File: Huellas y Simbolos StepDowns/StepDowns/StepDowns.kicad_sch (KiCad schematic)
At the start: 4 parts

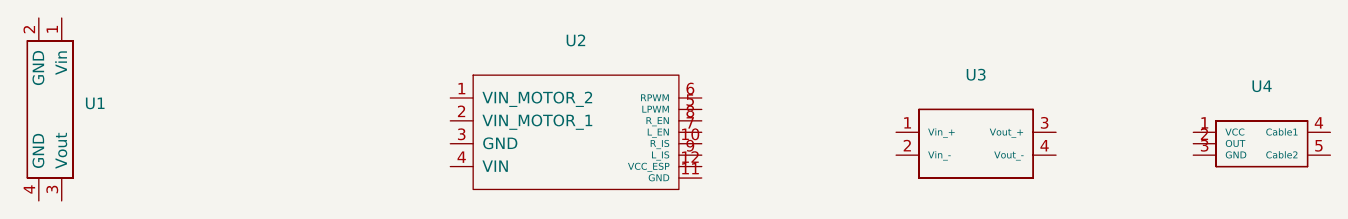
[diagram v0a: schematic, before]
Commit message: Se comenzó con la PCB para SALUS III
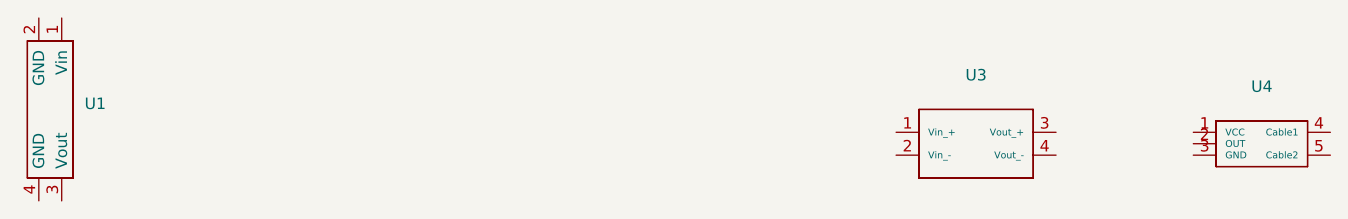
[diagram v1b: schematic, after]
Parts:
- removed U2: ~, Driver_Del_Motor:Driver_Motor, symbol Driver_Del_Motor:Driver_Motor
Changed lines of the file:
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@@
 	(paper "A4")
-	(symbol
-		(lib_id "Driver_Del_Motor:Driver_Motor")
-		(at 167.64 96.52 0)
-		(unit 1)
-		(exclude_from_sim no)
-		(in_bom yes)
-		(on_board yes)
-		(dnp no)
-		(fields_autoplaced yes)
-		(property "Reference" "U2"
-			(at 167.64 85.09 0)
-			(effects
-				(font
-					(size 1.27 1.27)
-				)
-			)
-		)
-		(property "Value" "~"
-			(at 167.64 87.63 0)
-			(effects
-				(font
-					(size 1.27 1.27)
-				)
-			)
-		)
-		(property "Footprint" "Driver_Del_Motor:Driver_Motor"
-			(at 167.64 96.52 0)
-			(effects
-				(font
-					(size 1.27 1.27)
-				)
-				(hide yes)
-			)
-		)
-		(property "Datasheet" ""
-			(at 167.64 96.52 0)
-			(effects
-				(font
-					(size 1.27 1.27)
-				)
-				(hide yes)
-			)
-		)
-		(property "Description" ""
-			(at 167.64 96.52 0)
-			(effects
-				(font
-					(size 1.27 1.27)
-				)
-				(hide yes)
-			)
-		)
-		(pin "6"
-		)
-		(pin "11"
-		)
-		(pin "12"
-		)
-		(pin "2"
-		)
-		(pin "8"
-		)
-		(pin "3"
-		)
-		(pin "4"
-		)
-		(pin "5"
-		)
-		(pin "7"
-		)
-		(pin "10"
-		)
-		(pin "9"
-		)
-		(pin "1"
-		)
-		(instances
-			(project ""
-				(path "/fa123d8e-0f61-4696-af24-c86f1c07897c"
-					(reference "U2")
-					(unit 1)
-				)
-			)
-		)
-	)
 	(symbol
 		(lib_id "Step_Chino:Step_Down_Chino")
